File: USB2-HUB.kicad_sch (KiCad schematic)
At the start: 31 parts, among them IC7 TPS2553QDBVRQ1, J4 USB_C_Receptacle_USB2.0_16P, U3 FSUSB42MUX, U4 TUSB4041IPAPQ1, Y1 24MHz Crystal

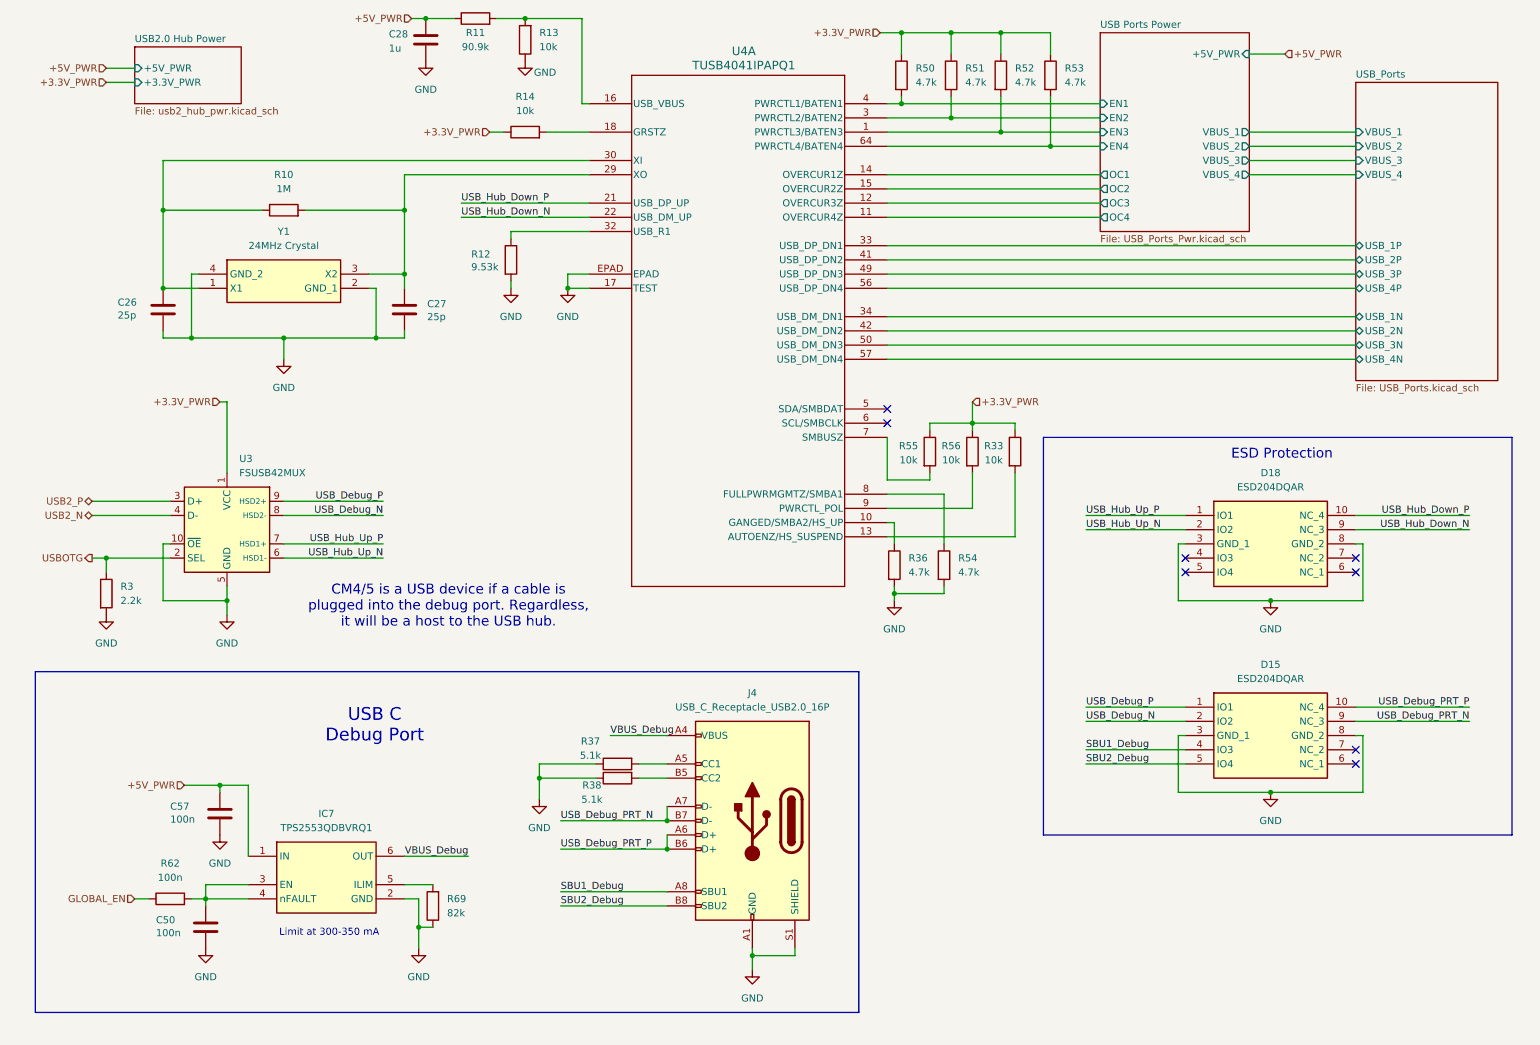
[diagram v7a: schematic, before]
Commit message: changed usb to be simpler (no inbuilt hub)
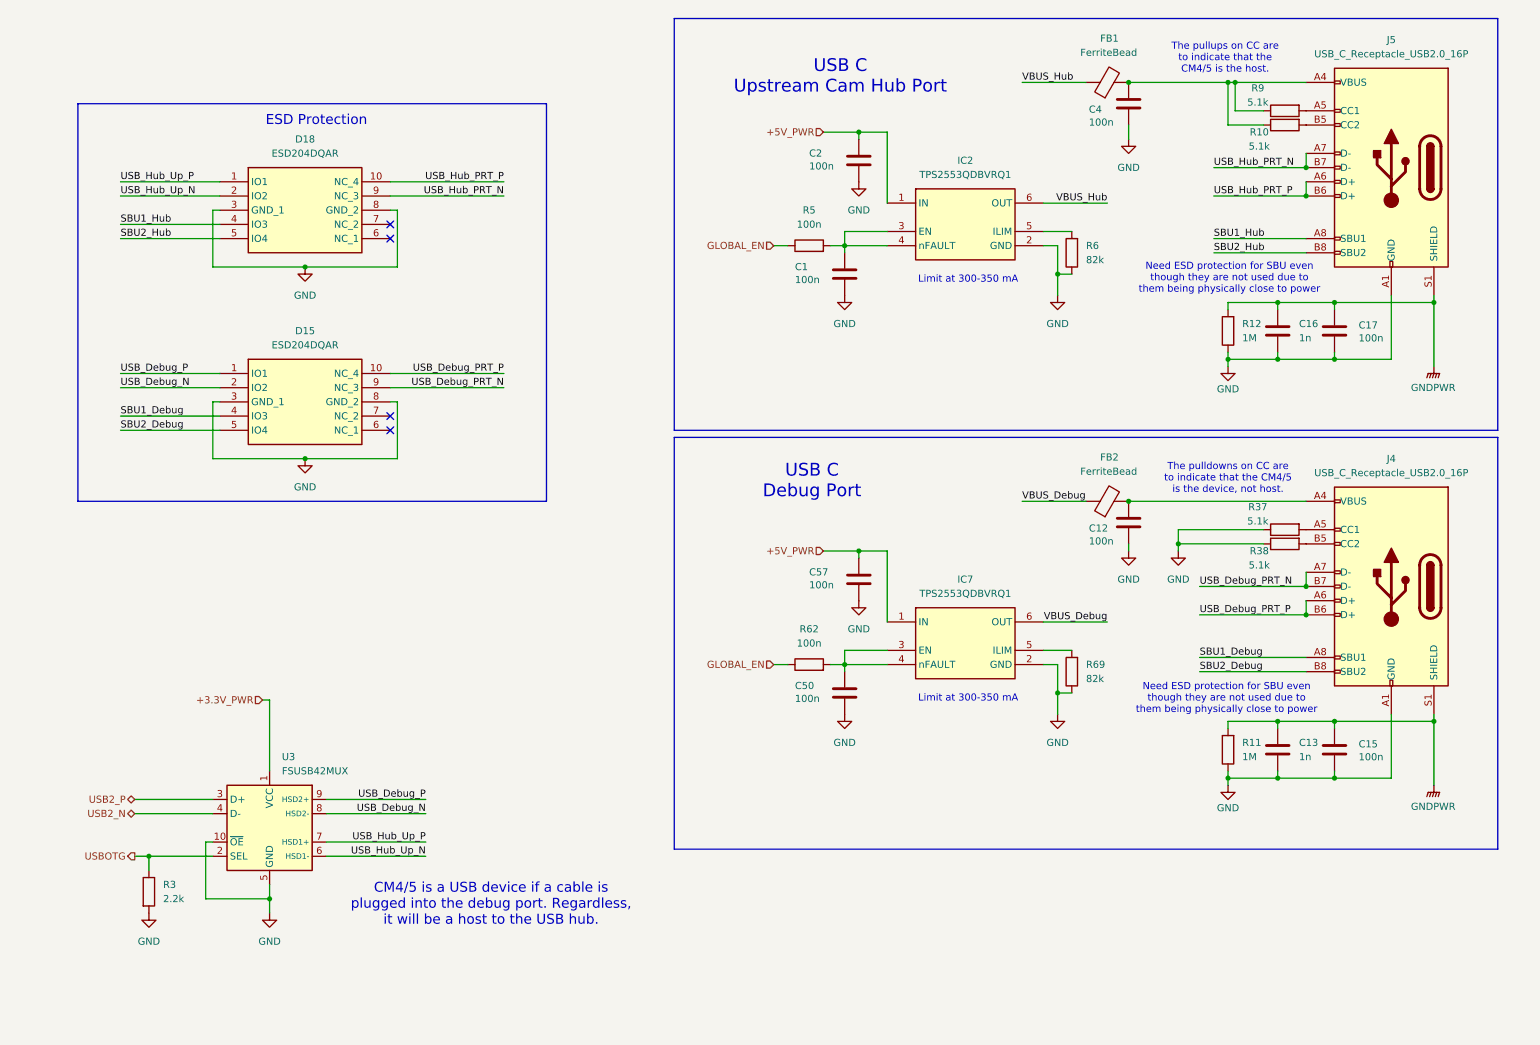
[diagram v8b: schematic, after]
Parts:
- removed C26, C27: 25p, Capacitor_SMD:C_0805_2012Metric, symbol Device:C
- removed C28: 1u, Capacitor_SMD:C_0805_2012Metric, symbol Device:C
- removed R13, R14, R33, R55, R56: 10k, Resistor_SMD:R_0805_2012Metric, symbol Device:R
- removed R36, R50, R51, R52, R53, R54: 4.7k, Resistor_SMD:R_0805_2012Metric, symbol Device:R
- removed U4: TUSB4041IPAPQ1, Controls_Pi:PAP64_4P15X4P15_TEX, symbol TUSB4041I-Q1:TUSB4041IPAPQ1
- removed Y1: 24MHz Crystal, Controls_Pi:ABM8AIG25000MHZ122ZT3, symbol ABM8AIG-24.000MHZ-12-2Z-T3:ABM8AIG-24.000MHZ-12-2Z-T3
- added C1, C12, C15, C17, C2, C4: 100n, Capacitor_SMD:C_0805_2012Metric, symbol Device:C
- added C13, C16: 1n, Capacitor_SMD:C_0805_2012Metric, symbol Device:C
- added FB1, FB2: FerriteBead, Inductor_SMD:L_1206_3216Metric, symbol Device:FerriteBead
- added IC2: TPS2553QDBVRQ1, Controls_Pi:SOT95P280X145-6N, symbol TPS2553QDBVRQ1:TPS2553QDBVRQ1
- added J5: USB_C_Receptacle_USB2.0_16P, symbol Connector:USB_C_Receptacle_USB2.0_16P
- added R5: 100n, Resistor_SMD:R_0805_2012Metric, symbol Device:R
- added R6: 82k, Resistor_SMD:R_0805_2012Metric, symbol Device:R
- added R9: 5.1k, Resistor_SMD:R_0805_2012Metric, symbol Device:R
- D15, D18: Arrow Part Number ESD204DQAR -> (none); Arrow Price/Stock https://www.arrow.com/en/products/esd204dqar/texas-instrume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 -> (none); Height 0.55 -> (none); Manufacturer_Name Texas Instruments -> (none); Manufacturer_Part_Number ESD204DQAR -> (none); Mouser Part Number 595-ESD204DQAR -> (none); Mouser Price/Stock https://www.mouser.co.uk/ProductDetail/Texas-Instruments/ES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 -> (none)
- IC7: Arrow Part Number TPS2553QDBVRQ1 -> (none); Arrow Price/Stock https://www.arrow.com/en/products/tps2553qdbvrq1/texas-inst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 -> (none); Height 1.45 -> (none); Manufacturer_Name Texas Instruments -> (none); Manufacturer_Part_Number TPS2553QDBVRQ1 -> (none); Mouser Part Number 595-TPS2553QDBVRQ1 -> (none); Mouser Price/Stock https://www.mouser.co.uk/ProductDetail/Texas-Instruments/TP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 -> (none)
- R10: value 1M -> 5.1k; P/N CRCW08051M00FKEA -> (none)
- R11: value 90.9k -> 1M; P/N CRCW080590K9FKEA -> CRCW08051M00FKEA
- R12: value 9.53k -> 1M; P/N RC0805FR-079K53L -> CRCW08051M00FKEA
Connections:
- net +5V_PWR: now also C2.1, IC2.1 (IN); no longer R11.1
- net GLOBAL_EN: now also R5.1
- net GND: now also R11.1, R12.1, C1.2, C12.2, C13.2, C15.2, C16.2, C17.2, C2.2, C4.2, IC2.2 (GND), J5.A1 (GND), J5.A12 (GND), J5.B1 (GND), J5.B12 (GND), R6.1; no longer J4.S1 (SHIELD), R12.2
- net VBUS_Debug: now also FB2.1; no longer J4.A4 (VBUS), J4.A9 (VBUS), J4.B4 (VBUS), J4.B9 (VBUS)
- net at R10.1: now also C4.1, FB1.2, J5.A4 (VBUS), J5.A9 (VBUS), J5.B4 (VBUS), J5.B9 (VBUS), R9.1
- net at R10.2: now also J5.B5 (CC2)
- net SBU1_Hub: now reaches D18.4 (IO3)
- net SBU1_Hub: now also J5.A8 (SBU1)
- net SBU2_Hub: now reaches D18.5 (IO4)
- net SBU2_Hub: now also J5.B8 (SBU2)
- net GNDPWR: now reaches R11.2
- net GNDPWR: now also J4.S1 (SHIELD), R12.2, C13.1, C15.1, C16.1, C17.1, J5.S1 (SHIELD)
- net USB_Hub_Down_N renamed USB_Hub_PRT_N
- net USB_Hub_PRT_N: now also J5.A7 (D-), J5.B7 (D-)
- net USB_Hub_Down_P renamed USB_Hub_PRT_P
- net USB_Hub_PRT_P: now also J5.A6 (D+), J5.B6 (D+)
- new net: J5.A5 (CC1), R9.2
- new net: C1.1, IC2.3 (EN), IC2.4 (nFAULT), R5.2
- new net: IC2.5 (ILIM), R6.2
- new net: C12.1, FB2.2, J4.A4 (VBUS), J4.A9 (VBUS), J4.B4 (VBUS), J4.B9 (VBUS)
- new net VBUS_Hub: FB1.1, IC2.6 (OUT)
- no-connect marks 8 -> 4
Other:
- removed sheet USB Ports Power
- removed sheet USB2.0 Hub Power
- removed sheet USB_Ports
- note added: "Need ESD protection for SBU even though they are not used due to them being physically close to power"
- note added: "The pulldowns on CC are to indicate that the CM4/5 is the device, not host."
- note added: "The pullups on CC are to indicate that the CM4/5 is the host."
- note added: "USB C Upstream Cam Hub Port"
- moved on the sheet: C50, C57, D15, D18, IC7, J4, R3, R37, R38, R62, R69, U3
